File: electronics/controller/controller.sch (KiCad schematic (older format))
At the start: 15 parts

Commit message: Add BJT solenoid driver
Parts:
- removed D?: LED, symbol LED
- removed R?: 1k, symbol R
- added D?: D, symbol D
- added L?: INDUCTOR, symbol INDUCTOR
- added Q?: TIP120, TO-220, symbol TIP120
- added R?: 10k, symbol R
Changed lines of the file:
@@
-$Comp
-L R R?
-U 1 1 56D7F277
-P 5550 4000
-F 0 "R?" V 5630 4000 50  0000 C CNN
-F 1 "1k" V 5550 4000 50  0000 C CNN
-F 2 "" V 5480 4000 50  0000 C CNN
-F 3 "" H 5550 4000 50  0000 C CNN
-	1    5550 4000
-	0    1    1    0
-$EndComp
 $Comp
 L R R?
@@
 $EndComp
 $Comp
-L LED D?
-U 1 1 56D7FC5C
-P 5100 4000
-F 0 "D?" H 5100 4100 50  0000 C CNN
-F 1 "LED" H 5100 3900 50  0000 C CNN
-F 2 "" H 5100 4000 50  0000 C CNN
-F 3 "" H 5100 4000 50  0000 C CNN
-	1    5100 4000
-	1    0    0    -1
-$EndComp
-$Comp
-L VCC #PWR?
-U 1 1 56D7FD5B
-P 5800 3900
-F 0 "#PWR?" H 5800 3750 50  0001 C CNN
-F 1 "VCC" H 5800 4050 50  0000 C CNN
-F 2 "" H 5800 3900 50  0000 C CNN
-F 3 "" H 5800 3900 50  0000 C CNN
-	1    5800 3900
-	1    0    0    -1
-$EndComp
-$Comp
 L VCC #PWR?
 U 1 1 56D7FDB7
@@
 L GND #PWR?
 U 1 1 56D89A81
-P 8800 3200
-F 0 "#PWR?" H 8800 2950 50  0001 C CNN
-F 1 "GND" H 8800 3050 50  0000 C CNN
-F 2 "" H 8800 3200 50  0000 C CNN
-F 3 "" H 8800 3200 50  0000 C CNN
-	1    8800 3200
+P 8800 3100
+F 0 "#PWR?" H 8800 2850 50  0001 C CNN
+F 1 "GND" H 8800 2950 50  0000 C CNN
+F 2 "" H 8800 3100 50  0000 C CNN
+F 3 "" H 8800 3100 50  0000 C CNN
+	1    8800 3100
 	1    0    0    -1
 $EndComp
@@
 $EndComp
 Wire Wire Line
-	1800 2800 1800 2900
-Wire Wire Line
-	1800 2900 1800 3850
+	1800 2800 1800 3850
 Wire Wire Line
 	1800 2900 1900 2900
@@
 	1900 4150 1700 4150
 Wire Wire Line
-	1700 3200 1700 4150
-Wire Wire Line
-	1700 4150 1700 4250
+	1700 3200 1700 4250
 Wire Wire Line
 	1900 3200 1700 3200
 Connection ~ 1700 4150
 Wire Wire Line
-	5700 4000 5800 4000
-Wire Wire Line
-	5800 4000 5800 3900
-Wire Wire Line
-	5400 4000 5300 4000
-Wire Wire Line
 	8300 3700 8300 3700
 Wire Wire Line
@@
 	6900 3950 6900 4200
 Wire Wire Line
-	6900 4200 6900 4200
-Wire Wire Line
 	6900 4400 6700 4400
 Wire Wire Line
@@
 	6000 1900 6000 2000
 Wire Wire Line
-	5900 1700 6000 1700
-Wire Wire Line
-	6000 1700 6100 1700
+	5900 1700 6100 1700
 Wire Wire Line
 	6000 1700 6000 1650
 Wire Wire Line
-	5900 1300 5950 1300
-Wire Wire Line
-	5950 1300 6000 1300
+	5900 1300 6000 1300
 Connection ~ 5950 1300
 Connection ~ 6000 1700
 Wire Wire Line
-	4700 1900 4800 1900
-Wire Wire Line
-	4800 1900 4900 1900
+	4700 1900 4900 1900
 Wire Wire Line
 	4800 1900 4800 1850
 Wire Wire Line
-	4700 1500 4800 1500
-Wire Wire Line
-	4800 1500 4900 1500
+	4700 1500 4900 1500
 Wire Wire Line
 	4800 1500 4800 1550
@@
 	8800 3000 8800 3100
 Wire Wire Line
-	8800 3100 8800 3200
-Wire Wire Line
-	8800 2400 8800 2550
-Wire Wire Line
-	8800 2550 8800 2600
+	8800 2400 8800 2600
 Wire Wire Line
 	8800 2550 9200 2550
 Connection ~ 8800 2550
 Wire Wire Line
-	8400 3100 8800 3100
+	8800 3100 8400 3100
 Connection ~ 8800 3100
 Wire Wire Line
-	8300 2800 8400 2800
-Wire Wire Line
-	8400 2800 8500 2800
+	8300 2800 8500 2800
 Connection ~ 8400 2800
 Wire Wire Line
@@
 Wire Wire Line
 	8800 1950 8800 2100
+$Comp
+L TIP120 Q?
+U 1 1 56D91017
+P 8800 4200
+F 0 "Q?" H 9050 4275 50  0000 L CNN
+F 1 "TIP120" H 9050 4200 50  0000 L CNN
+F 2 "TO-220" H 9050 4125 50  0000 L CIN
+F 3 "" H 8800 4200 50  0000 L CNN
+	1    8800 4200
+	1    0    0    -1
+$EndComp
+$Comp
+L D D?
+U 1 1 56D9128D
+P 8900 3750
+F 0 "D?" H 8900 3850 50  0000 C CNN
+F 1 "D" H 8900 3650 50  0000 C CNN
+F 2 "" H 8900 3750 50  0000 C CNN
+F 3 "" H 8900 3750 50  0000 C CNN
+	1    8900 3750
+	0    1    1    0
+$EndComp
+$Comp
+L R R?
+U 1 1 56D91400
+P 8450 4200
+F 0 "R?" V 8530 4200 50  0000 C CNN
+F 1 "10k" V 8450 4200 50  0000 C CNN
+F 2 "" V 8380 4200 50  0000 C CNN
+F 3 "" H 8450 4200 50  0000 C CNN
+	1    8450 4200
+	0    1    1    0
+$EndComp
+$Comp
+L +24V #PWR?
+U 1 1 56D919AD
+P 8900 3500
+F 0 "#PWR?" H 8900 3350 50  0001 C CNN
+F 1 "+24V" H 8900 3640 50  0000 C CNN
+F 2 "" H 8900 3500 50  0000 C CNN
+F 3 "" H 8900 3500 50  0000 C CNN
+	1    8900 3500
+	1    0    0    -1
+$EndComp
+$Comp
+L GND #PWR?
+U 1 1 56D91AA2
+P 8900 4400
+F 0 "#PWR?" H 8900 4150 50  0001 C CNN
+F 1 "GND" H 8900 4250 50  0000 C CNN
+F 2 "" H 8900 4400 50  0000 C CNN
+F 3 "" H 8900 4400 50  0000 C CNN
+	1    8900 4400
+	1    0    0    -1
+$EndComp
+Wire Wire Line
+	8900 3500 8900 3600
+Wire Wire Line
+	8900 3900 8900 4000
+Wire Wire Line
+	8900 3550 9000 3550
+Connection ~ 8900 3550
+Wire Wire Line
+	8900 3950 9000 3950
+Connection ~ 8900 3950
+$Comp
+L INDUCTOR L?
+U 1 1 56D91FB7
+P 9200 3750
+F 0 "L?" V 9150 3750 50  0000 C CNN
+F 1 "INDUCTOR" V 9300 3750 50  0000 C CNN
+F 2 "" H 9200 3750 50  0000 C CNN
+F 3 "" H 9200 3750 50  0000 C CNN
+	1    9200 3750
+	1    0    0    -1
+$EndComp
+Wire Wire Line
+	9200 4050 9000 4050
+Wire Wire Line
+	9000 4050 9000 3950
+Wire Wire Line
+	9000 3550 9000 3450
+Wire Wire Line
+	9000 3450 9200 3450
+Wire Wire Line
+	4300 3850 6600 3850
+Wire Wire Line
+	6600 3850 6600 2800
+Wire Wire Line
+	6600 2800 6900 2800
+Wire Wire Line
+	4300 4850 6100 4850
+Wire Wire Line
+	6100 4850 6100 1700
 $EndSCHEMATC

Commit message: Move shift registers to solenoid driver
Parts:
- removed U? (x2): 74HC595, symbol 74HC595
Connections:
- wire segments 50 -> 38
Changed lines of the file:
@@
-$EndComp
-$Comp
-L 74HC595 U?
-U 1 1 56D802EF
-P 7600 3250
-F 0 "U?" H 7750 3850 50  0000 C CNN
-F 1 "74HC595" H 7600 2650 50  0000 C CNN
-F 2 "" H 7600 3250 50  0000 C CNN
-F 3 "" H 7600 3250 50  0000 C CNN
-	1    7600 3250
-	1    0    0    -1
-$EndComp
-$Comp
-L 74HC595 U?
-U 1 1 56D80414
-P 7600 4650
-F 0 "U?" H 7750 5250 50  0000 C CNN
-F 1 "74HC595" H 7600 4050 50  0000 C CNN
-F 2 "" H 7600 4650 50  0000 C CNN
-F 3 "" H 7600 4650 50  0000 C CNN
-	1    7600 4650
-	1    0    0    -1
 $EndComp
 $Comp
@@
 Connection ~ 1700 4150
 Wire Wire Line
-	8300 3700 8300 3700
-Wire Wire Line
-	8300 3700 8300 3950
-Wire Wire Line
-	8300 3950 6900 3950
-Wire Wire Line
-	6900 3950 6900 4200
-Wire Wire Line
-	6900 4400 6700 4400
-Wire Wire Line
-	6700 4400 6700 3000
-Wire Wire Line
-	6700 3000 6900 3000
-Wire Wire Line
-	6900 3300 6800 3300
-Wire Wire Line
-	6800 3300 6800 4700
-Wire Wire Line
-	6800 4700 6900 4700
-Wire Wire Line
 	5900 1500 5900 1500
 Wire Wire Line
@@
 Wire Wire Line
 	8300 2800 8500 2800
-Connection ~ 8400 2800
 Wire Wire Line
 	9200 1900 9200 1950
@@
 	4300 3850 6600 3850
 Wire Wire Line
-	6600 3850 6600 2800
-Wire Wire Line
-	6600 2800 6900 2800
-Wire Wire Line
 	4300 4850 6100 4850
 Wire Wire Line
 	6100 4850 6100 1700
+Connection ~ 8400 2800
 $EndSCHEMATC

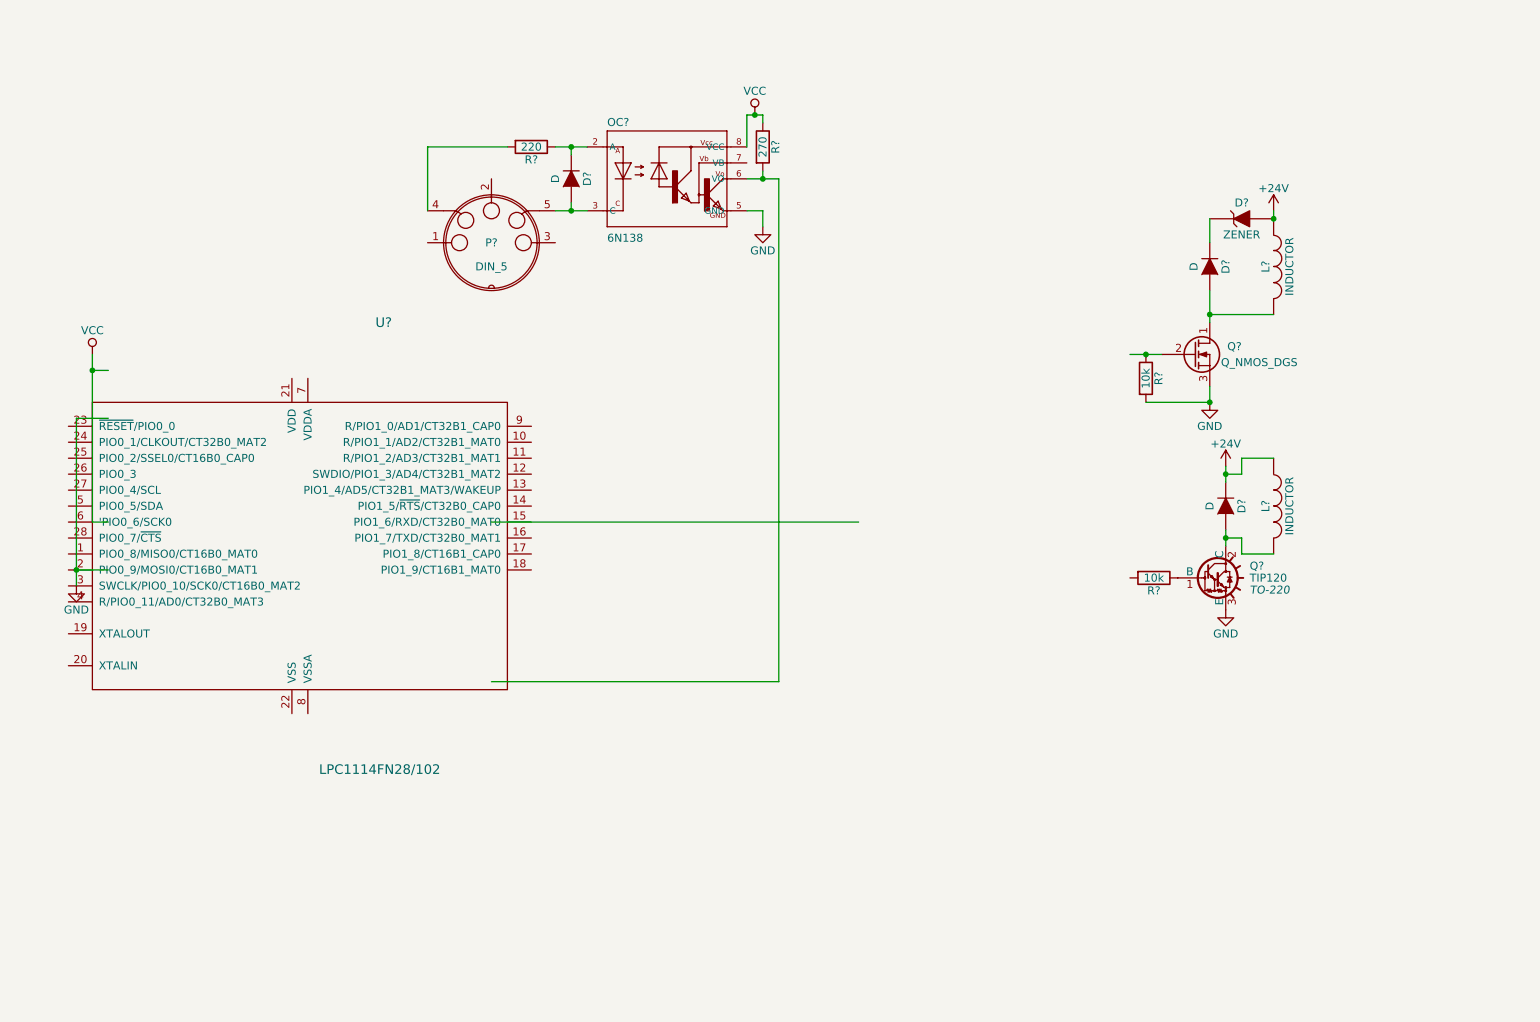
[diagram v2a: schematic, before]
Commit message: Add JTAG connector
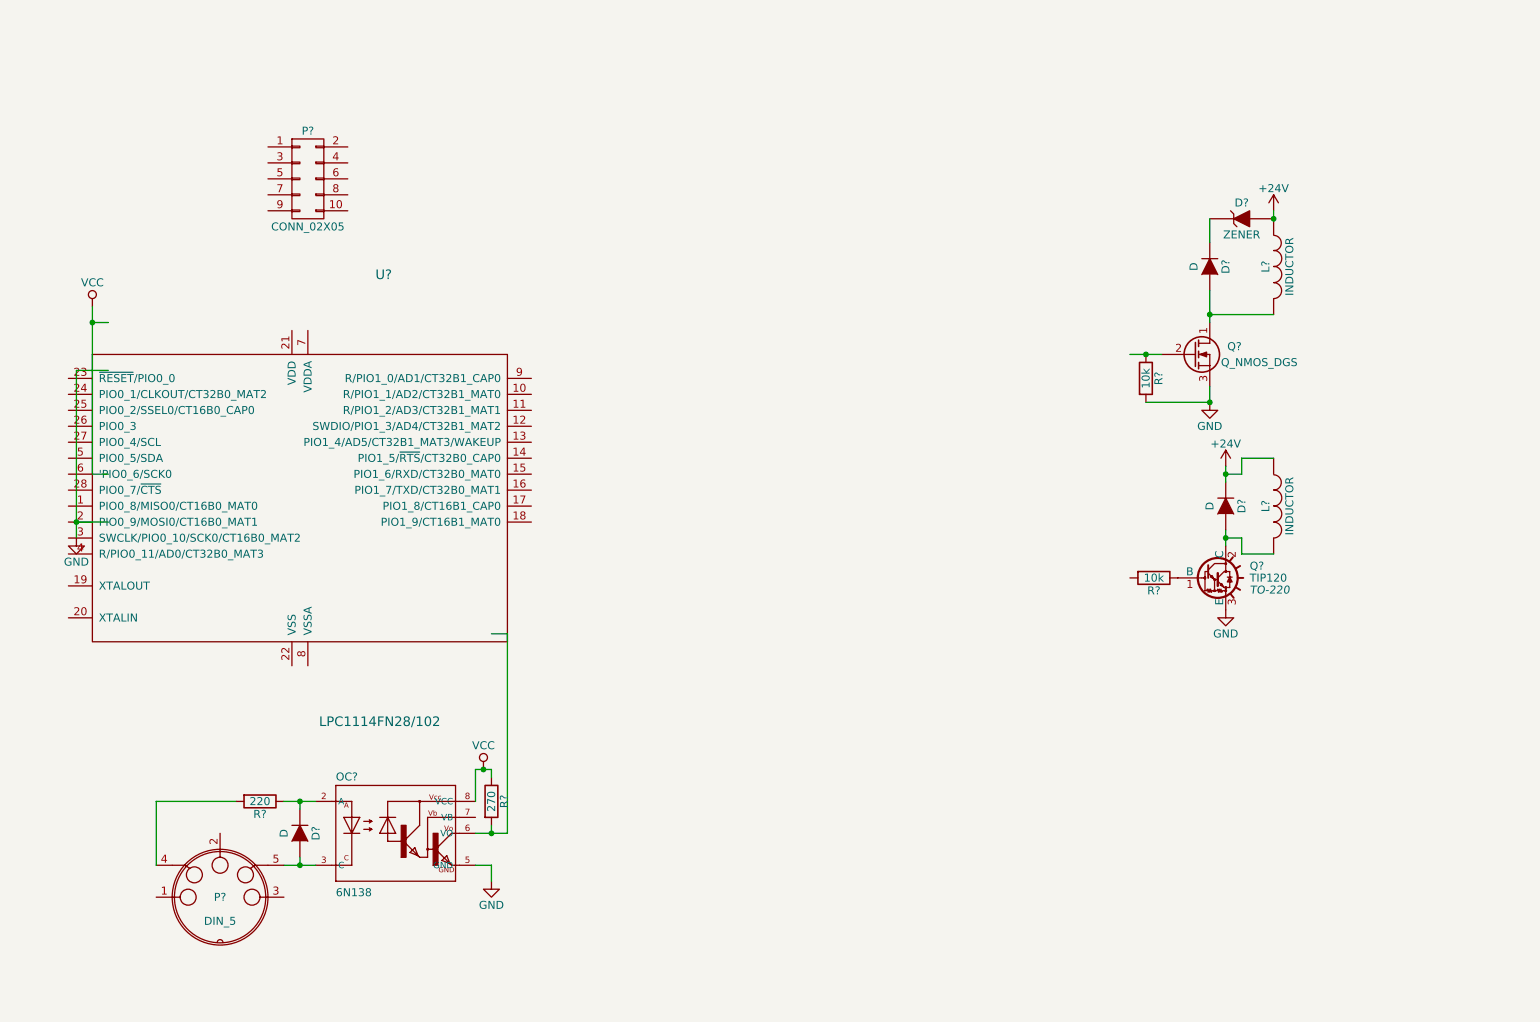
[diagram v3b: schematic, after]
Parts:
- added P?: CONN_02X05, symbol CONN_02X05
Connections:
- wire segments 38 -> 47
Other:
- moved on the sheet: D?, OC?, P?, R?, U?
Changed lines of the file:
@@
 L R R?
 U 1 1 56D7F762
-P 6000 1500
-F 0 "R?" V 6080 1500 50  0000 C CNN
-F 1 "270" V 6000 1500 50  0000 C CNN
-F 2 "" V 5930 1500 50  0000 C CNN
-F 3 "" H 6000 1500 50  0000 C CNN
-	1    6000 1500
+P 4300 5600
+F 0 "R?" V 4380 5600 50  0000 C CNN
+F 1 "270" V 4300 5600 50  0000 C CNN
+F 2 "" V 4230 5600 50  0000 C CNN
+F 3 "" H 4300 5600 50  0000 C CNN
+	1    4300 5600
 	1    0    0    -1
 $EndComp
@@
 L LPC1114FN28/102 U?
 U 1 1 56D7F9F7
-P 3100 4000
-F 0 "U?" H 3625 5400 60  0000 C CNN
-F 1 "LPC1114FN28/102" H 3600 2600 60  0000 C CNN
-F 2 "" H 3100 4000 60  0000 C CNN
-F 3 "" H 3100 4000 60  0000 C CNN
-	1    3100 4000
+P 3100 3700
+F 0 "U?" H 3625 5100 60  0000 C CNN
+F 1 "LPC1114FN28/102" H 3600 2300 60  0000 C CNN
+F 2 "" H 3100 3700 60  0000 C CNN
+F 3 "" H 3100 3700 60  0000 C CNN
+	1    3100 3700
 	1    0    0    -1
 $EndComp
@@
 L VCC #PWR?
 U 1 1 56D7FDB7
-P 1800 2800
-F 0 "#PWR?" H 1800 2650 50  0001 C CNN
-F 1 "VCC" H 1800 2950 50  0000 C CNN
-F 2 "" H 1800 2800 50  0000 C CNN
-F 3 "" H 1800 2800 50  0000 C CNN
-	1    1800 2800
+P 1800 2500
+F 0 "#PWR?" H 1800 2350 50  0001 C CNN
+F 1 "VCC" H 1800 2650 50  0000 C CNN
+F 2 "" H 1800 2500 50  0000 C CNN
+F 3 "" H 1800 2500 50  0000 C CNN
+	1    1800 2500
 	1    0    0    -1
 $EndComp
@@
 L GND #PWR?
 U 1 1 56D7FDD3
-P 1700 4250
-F 0 "#PWR?" H 1700 4000 50  0001 C CNN
-F 1 "GND" H 1700 4100 50  0000 C CNN
-F 2 "" H 1700 4250 50  0000 C CNN
-F 3 "" H 1700 4250 50  0000 C CNN
-	1    1700 4250
-	1    0    0    -1
-$EndComp
-$Comp
-L DIN_5 P?
-U 1 1 56D8006A
-P 4300 2100
-F 0 "P?" H 4300 2100 50  0000 C CNN
-F 1 "DIN_5" H 4300 1950 50  0000 C CNN
-F 2 "" H 4300 2100 50  0000 C CNN
-F 3 "" H 4300 2100 50  0000 C CNN
-	1    4300 2100
+P 1700 3950
+F 0 "#PWR?" H 1700 3700 50  0001 C CNN
+F 1 "GND" H 1700 3800 50  0000 C CNN
+F 2 "" H 1700 3950 50  0000 C CNN
+F 3 "" H 1700 3950 50  0000 C CNN
+	1    1700 3950
 	1    0    0    -1
 $EndComp
@@
 L 6N138 OC?
 U 1 1 56D87D42
-P 5400 1700
-F 0 "OC?" H 5025 2025 50  0000 L BNN
-F 1 "6N138" H 5025 1300 50  0000 L BNN
-F 2 "optocoupler-DIL08" H 5400 1850 50  0001 C CNN
-F 3 "" H 5400 1700 60  0000 C CNN
-	1    5400 1700
+P 3700 5800
+F 0 "OC?" H 3325 6125 50  0000 L BNN
+F 1 "6N138" H 3325 5400 50  0000 L BNN
+F 2 "optocoupler-DIL08" H 3700 5950 50  0001 C CNN
+F 3 "" H 3700 5800 60  0000 C CNN
+	1    3700 5800
 	1    0    0    -1
 $EndComp
@@
 L VCC #PWR?
 U 1 1 56D87E1C
-P 5950 1300
-F 0 "#PWR?" H 5950 1150 50  0001 C CNN
-F 1 "VCC" H 5950 1450 50  0000 C CNN
-F 2 "" H 5950 1300 50  0000 C CNN
-F 3 "" H 5950 1300 50  0000 C CNN
-	1    5950 1300
+P 4250 5400
+F 0 "#PWR?" H 4250 5250 50  0001 C CNN
+F 1 "VCC" H 4250 5550 50  0000 C CNN
+F 2 "" H 4250 5400 50  0000 C CNN
+F 3 "" H 4250 5400 50  0000 C CNN
+	1    4250 5400
 	1    0    0    -1
 $EndComp
@@
 L GND #PWR?
 U 1 1 56D8803F
-P 6000 2000
-F 0 "#PWR?" H 6000 1750 50  0001 C CNN
-F 1 "GND" H 6000 1850 50  0000 C CNN
-F 2 "" H 6000 2000 50  0000 C CNN
-F 3 "" H 6000 2000 50  0000 C CNN
-	1    6000 2000
+P 4300 6100
+F 0 "#PWR?" H 4300 5850 50  0001 C CNN
+F 1 "GND" H 4300 5950 50  0000 C CNN
+F 2 "" H 4300 6100 50  0000 C CNN
+F 3 "" H 4300 6100 50  0000 C CNN
+	1    4300 6100
 	1    0    0    -1
 $EndComp
@@
 L D D?
 U 1 1 56D883DA
-P 4800 1700
-F 0 "D?" H 4800 1800 50  0000 C CNN
-F 1 "D" H 4800 1600 50  0000 C CNN
-F 2 "" H 4800 1700 50  0000 C CNN
-F 3 "" H 4800 1700 50  0000 C CNN
-	1    4800 1700
+P 3100 5800
+F 0 "D?" H 3100 5900 50  0000 C CNN
+F 1 "D" H 3100 5700 50  0000 C CNN
+F 2 "" H 3100 5800 50  0000 C CNN
+F 3 "" H 3100 5800 50  0000 C CNN
+	1    3100 5800
 	0    1    1    0
 $EndComp
@@
 L R R?
 U 1 1 56D887F9
-P 4550 1500
-F 0 "R?" V 4630 1500 50  0000 C CNN
-F 1 "220" V 4550 1500 50  0000 C CNN
-F 2 "" V 4480 1500 50  0000 C CNN
-F 3 "" H 4550 1500 50  0000 C CNN
-	1    4550 1500
+P 2850 5600
+F 0 "R?" V 2930 5600 50  0000 C CNN
+F 1 "220" V 2850 5600 50  0000 C CNN
+F 2 "" V 2780 5600 50  0000 C CNN
+F 3 "" H 2850 5600 50  0000 C CNN
+	1    2850 5600
 	0    1    1    0
 $EndComp
@@
 $EndComp
 Wire Wire Line
-	1800 2800 1800 3850
-Wire Wire Line
-	1800 2900 1900 2900
-Wire Wire Line
-	1800 3850 1900 3850
-Connection ~ 1800 2900
-Wire Wire Line
-	1900 4150 1700 4150
-Wire Wire Line
-	1700 3200 1700 4250
-Wire Wire Line
-	1900 3200 1700 3200
-Connection ~ 1700 4150
-Wire Wire Line
-	5900 1500 5900 1500
-Wire Wire Line
-	5900 1500 5900 1300
-Wire Wire Line
-	5900 1900 6000 1900
-Wire Wire Line
-	6000 1900 6000 2000
-Wire Wire Line
-	5900 1700 6100 1700
-Wire Wire Line
-	6000 1700 6000 1650
-Wire Wire Line
-	5900 1300 6000 1300
-Connection ~ 5950 1300
-Connection ~ 6000 1700
-Wire Wire Line
-	4700 1900 4900 1900
-Wire Wire Line
-	4800 1900 4800 1850
-Wire Wire Line
-	4700 1500 4900 1500
-Wire Wire Line
-	4800 1500 4800 1550
-Connection ~ 4800 1500
-Connection ~ 4800 1900
-Wire Wire Line
-	4400 1500 3900 1500
-Wire Wire Line
-	3900 1500 3900 1900
-Wire Wire Line
-	6000 1300 6000 1350
+	1800 2500 1800 2600
+Wire Wire Line
+	1800 2600 1800 3550
+Wire Wire Line
+	1800 2600 1900 2600
+Wire Wire Line
+	1800 3550 1900 3550
+Connection ~ 1800 2600
+Wire Wire Line
+	1900 3850 1700 3850
+Wire Wire Line
+	1700 2900 1700 3850
+Wire Wire Line
+	1700 3850 1700 3950
+Wire Wire Line
+	1900 2900 1700 2900
+Connection ~ 1700 3850
+Wire Wire Line
+	4200 5600 4200 5600
+Wire Wire Line
+	4200 5600 4200 5400
+Wire Wire Line
+	4200 6000 4300 6000
+Wire Wire Line
+	4300 6000 4300 6100
+Wire Wire Line
+	4200 5800 4300 5800
+Wire Wire Line
+	4300 5800 4400 5800
+Wire Wire Line
+	4300 5800 4300 5750
+Wire Wire Line
+	4200 5400 4250 5400
+Wire Wire Line
+	4250 5400 4300 5400
+Connection ~ 4250 5400
+Connection ~ 4300 5800
+Wire Wire Line
+	3000 6000 3100 6000
+Wire Wire Line
+	3100 6000 3200 6000
+Wire Wire Line
+	3100 6000 3100 5950
+Wire Wire Line
+	3000 5600 3100 5600
+Wire Wire Line
+	3100 5600 3200 5600
+Wire Wire Line
+	3100 5600 3100 5650
+Connection ~ 3100 5600
+Connection ~ 3100 6000
+Wire Wire Line
+	4300 5400 4300 5450
 Wire Wire Line
 	8800 3000 8800 3100
 Wire Wire Line
-	8800 2400 8800 2600
+	8800 2400 8800 2550
+Wire Wire Line
+	8800 2550 8800 2600
 Wire Wire Line
 	8800 2550 9200 2550
@@
 Connection ~ 8800 3100
 Wire Wire Line
-	8300 2800 8500 2800
+	8300 2800 8400 2800
+Wire Wire Line
+	8400 2800 8500 2800
 Wire Wire Line
 	9200 1900 9200 1950
@@
 $EndComp
 Wire Wire Line
-	8900 3500 8900 3600
-Wire Wire Line
-	8900 3900 8900 4000
+	8900 3500 8900 3550
+Wire Wire Line
+	8900 3550 8900 3600
+Wire Wire Line
+	8900 3900 8900 3950
+Wire Wire Line
+	8900 3950 8900 4000
 Wire Wire Line
 	8900 3550 9000 3550
@@
 	9000 3450 9200 3450
 Wire Wire Line
-	4300 3850 6600 3850
-Wire Wire Line
-	4300 4850 6100 4850
-Wire Wire Line
-	6100 4850 6100 1700
+	4300 4550 4400 4550
+Wire Wire Line
+	4400 4550 4400 5800
 Connection ~ 8400 2800
+$Comp
+L CONN_02X05 P?
+U 1 1 56DFB95F
+P 3150 1700
+F 0 "P?" H 3150 2000 50  0000 C CNN
+F 1 "CONN_02X05" H 3150 1400 50  0000 C CNN
+F 2 "" H 3150 500 50  0000 C CNN
+F 3 "" H 3150 500 50  0000 C CNN
+	1    3150 1700
+	1    0    0    -1
+$EndComp
+$Comp
+L DIN_5 P?
+U 1 1 56D8006A
+P 2600 6200
+F 0 "P?" H 2600 6200 50  0000 C CNN
+F 1 "DIN_5" H 2600 6050 50  0000 C CNN
+F 2 "" H 2600 6200 50  0000 C CNN
+F 3 "" H 2600 6200 50  0000 C CNN
+	1    2600 6200
+	1    0    0    -1
+$EndComp
+Wire Wire Line
+	2700 5600 2200 5600
+Wire Wire Line
+	2200 5600 2200 6000
 $EndSCHEMATC

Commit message: Add pin headers, power regulator, and barrel jack
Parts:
- added C?: 10u, symbol CP
- added C?: 1u, symbol C
- added CON?: BARREL_JACK, symbol BARREL_JACK
- added P?: SPI, symbol CONN_01X06
- added P?: I2C, symbol CONN_01X04
- added P?: USART, symbol CONN_01X04
- added P? (x2): CONN_01X14, symbol CONN_01X14
- added U?: LD3985G33R, TSOT-23-5, symbol LD3985G33R
- P?: value CONN_02X05 -> JTAG
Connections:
- net labels added: +3.3V, MISO, MOSI, PIO0_0, PIO0_1, PIO0_10, PIO0_11, PIO0_2, PIO0_3, PIO0_4, PIO0_5, PIO0_6, PIO0_7, PIO0_8, PIO0_9, PIO1_0, PIO1_1, PIO1_2, PIO1_3, PIO1_4, PIO1_5, PIO1_6, PIO1_7, PIO1_8, PIO1_9, RESET, RXD, SCK, SCL, SDA, SSEL, SWCLK, SWDIO, SWO, TXD
- wire segments 47 -> 143
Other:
- moved on the sheet: D?, L?, OC?, P?, Q?, R?, U?

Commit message: Update microcontroller and regulator components
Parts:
- removed U?: LPC1114FN28/102, symbol LPC1114FN28/102
- removed U?: LD3985G33R, TSOT-23-5, symbol LD3985G33R
- added U?: LPC1114FDH28/102, symbol LPC1114FDH28/102
- added U?: SPX3819M5-3.3, SOT-23-5, symbol SPX3819M5-3.3
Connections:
- wire segments 143 -> 120
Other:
- moved on the sheet: C?, CON?, P?
